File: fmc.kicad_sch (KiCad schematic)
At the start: 31 parts, among them P1 ASP-134488-01, Q1 FDN335N, Q2 FDN335N, Q3 FDN335N

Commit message: Revision based on pre-production
-Added pull-down on the OE for the Digital output buffers
- increase board edge (was 0.3mm, but via and traces are 0.5mm away now)
- move power vias away from board edge
- Increase power via size from 0.6mm/0.3mm to 0.8mm/0.4mm in a couple of places
- Naming of level shifter output enable changed to make function clear throughout the design.
- Revised SMPS layout slightly to better use the space.
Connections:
- net Cleaner_~{OE}_0 renamed Cleaner_LevelShift_~{OE}_0
- net Cleaner_~{OE}_1 renamed Cleaner_LevelShift_~{OE}_1
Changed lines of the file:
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@@
 	(wire
 		(pts
-			(xy 156.21 88.9) (xy 198.12 88.9)
+			(xy 152.4 88.9) (xy 198.12 88.9)
 		)
 		(stroke
@@
 		)
 	)
-	(label "Cleaner_~{OE}_1"
+	(label "Cleaner_LevelShift_~{OE}_1"
 		(at 86.36 114.3 180)
 		(effects
@@
 		)
 	)
-	(label "Cleaner_~{OE}_0"
+	(label "Cleaner_LevelShift_~{OE}_0"
 		(at 86.36 58.42 180)
 		(effects
@@
 		)
 	)
-	(label "Cleaner_~{OE}_1"
+	(label "Cleaner_LevelShift_~{OE}_1"
 		(at 360.68 80.01 0)
 		(effects
@@
 		)
 	)
-	(label "Cleaner_~{OE}_0"
-		(at 156.21 88.9 0)
+	(label "Cleaner_LevelShift_~{OE}_0"
+		(at 152.4 88.9 0)
 		(effects
 			(font
@@
 		)
 	)
-	(hierarchical_label "Cleaner_~{OE}_1"
+	(hierarchical_label "Cleaner_LevelShift_~{OE}_1"
 		(shape output)
 		(at 46.99 114.3 180)
@@
 		)
 	)
-	(hierarchical_label "Cleaner_~{OE}_0"
+	(hierarchical_label "Cleaner_LevelShift_~{OE}_0"
 		(shape output)
 		(at 46.99 58.42 180)

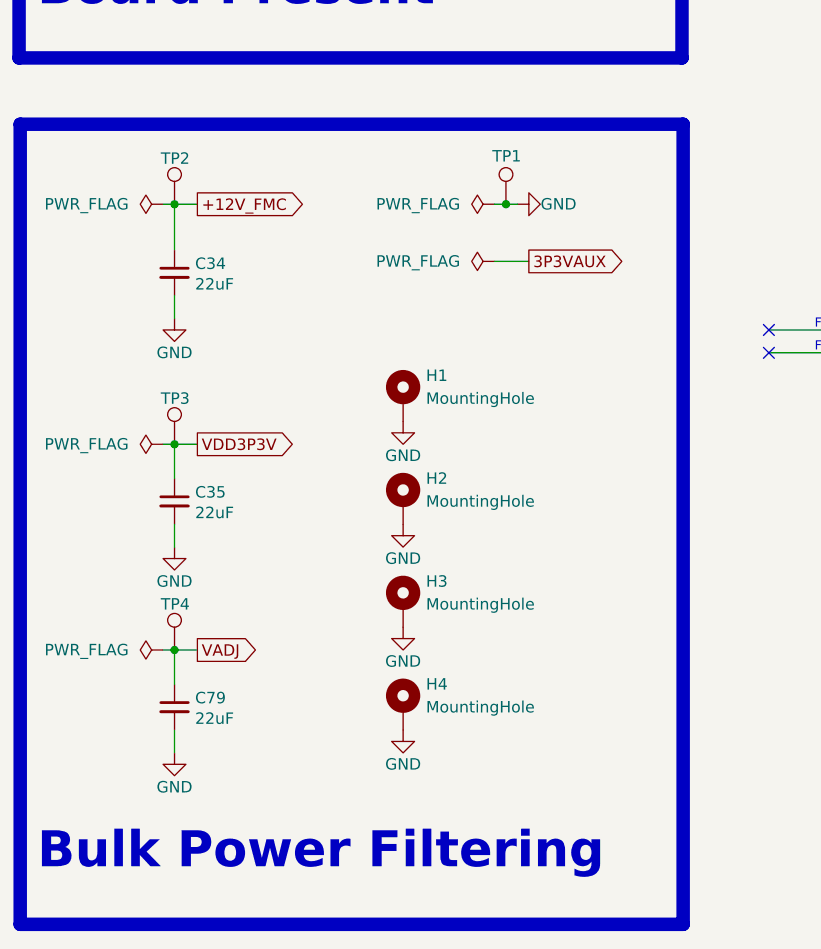
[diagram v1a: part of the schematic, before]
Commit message: Updates from Pre-production boards
- removed ground from mounting holes and added no-pop 0805 resistors to optionally ground the mounting holes.
- Adjusted placement of some test points.
- Made the test point loops non-populated parts, the pads will remain.
- Added silkscreen labels to the test points.
- Fixed pulldown resistor added in prevoius commit.
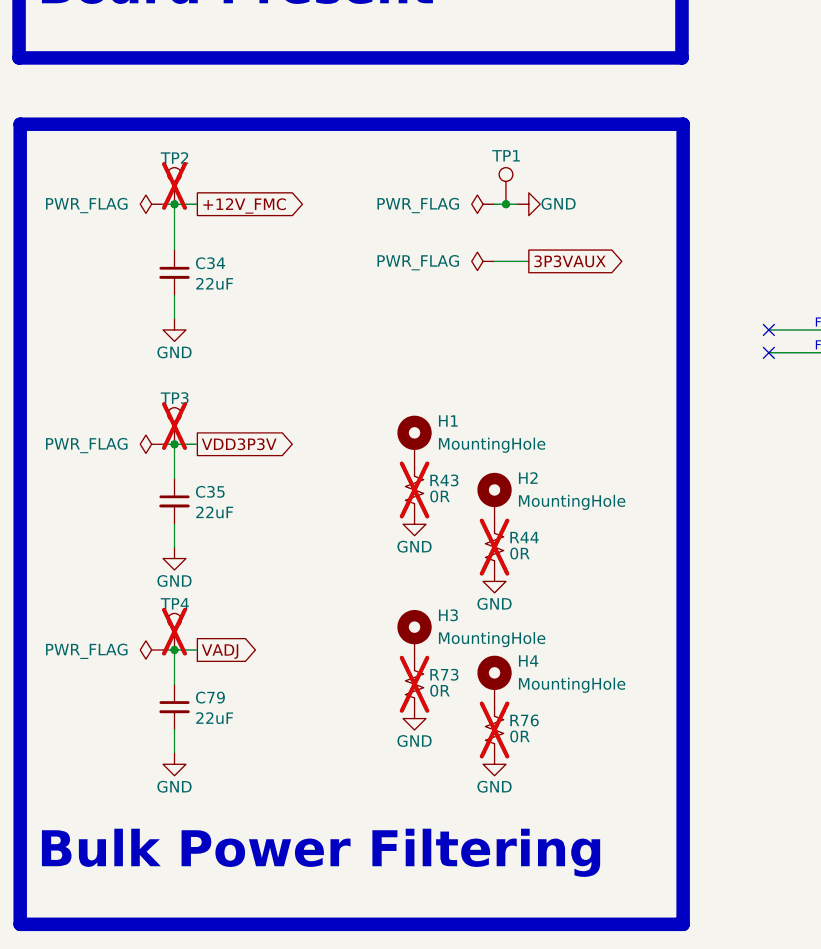
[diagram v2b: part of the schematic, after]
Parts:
- added R43, R44, R73, R76: 0R, Resistor_SMD:R_0805_2012Metric, symbol Device:R_Small_US
- TP2, TP3, TP4: now not fitted
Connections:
- net GND: now also R43.1, R44.1, R73.1, R76.1; no longer H1.1, H2.1, H3.1, H4.1
- new net: H3.1, R73.2
- new net: H4.1, R76.2
- new net: H1.1, R43.2
- new net: H2.1, R44.2
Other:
- moved on the sheet: H1, H2, H3, H4
